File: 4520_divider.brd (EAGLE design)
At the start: 99.4 x 30.5 mm, 54 parts, among them IC1 4520N, IC2 4050N, IC3 78L05Z

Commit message: Moved labels, added top layer ground plane, added alternative 1206 caps in PSU curcuit for use when low-profile electrolytic caps are hard to find.
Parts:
- added C4, C5: 10u, rcl:C1206K
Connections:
- net +5V: now also C5.1
- net GND: now also C4.2, C5.2
- net N$7: now also C4.1
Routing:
- net +5V: track 56.7 -> 59.4 mm
- net N$7: track 6.35 -> 9.12 mm
- added copper zone on layer 1, net GND
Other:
- board text added: "RED STRIPE <- -12V here"
- board text removed: "<-RED STRIPE/-12V HERE"
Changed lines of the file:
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@@
 <wire x1="84.455" y1="5.715" x2="84.455" y2="1.905" width="0.254" layer="22"/>
 <wire x1="85.09" y1="6.35" x2="85.09" y2="1.27" width="0.254" layer="22"/>
-<text x="83.185" y="4.445" size="1.27" layer="22" font="vector" rot="SMR0">&lt;-RED STRIPE/-12V HERE</text>
-<text x="81.915" y="18.415" size="1.27" layer="22" font="vector" rot="SMR0">4520 clock divider
+<text x="83.185" y="4.445" size="1.4224" layer="22" font="vector" rot="SMR0">RED STRIPE
+&lt;- -12V here</text>
+<text x="80.645" y="17.78" size="1.016" layer="22" font="vector" rot="SMR0">4520 clock divider
 cc-by-sa 2016
 Lars Bengtsson</text>
@@
 <attribute name="VALUE" x="51.816" y="5.334" size="1.27" layer="27" ratio="10" rot="R180"/>
 </element>
-<element name="D1" library="diode" package="D-2.5" value="" x="96.52" y="7.62"/>
+<element name="D1" library="diode" package="D-2.5" value="" x="96.52" y="7.62" smashed="yes">
+<attribute name="NAME" x="96.774" y="8.763" size="1.27" layer="25" ratio="10"/>
+<attribute name="VALUE" x="94.869" y="5.207" size="1.27" layer="27" ratio="10"/>
+</element>
 <element name="IC1" library="45xx" package="DIL16" value="4520N" x="54.61" y="13.97" smashed="yes" rot="R90">
 <attribute name="NAME" x="57.531" y="3.429" size="1.27" layer="25" ratio="10" rot="R180"/>
 <attribute name="VALUE" x="55.245" y="10.922" size="1.27" layer="25" ratio="10" rot="R90"/>
 </element>
-<element name="IC3" library="linear" package="TO92" value="78L05Z" x="91.44" y="7.62"/>
+<element name="IC3" library="linear" package="TO92" value="78L05Z" x="91.44" y="7.62" smashed="yes">
+<attribute name="NAME" x="88.519" y="6.858" size="1.27" layer="25" ratio="10" rot="R90"/>
+<attribute name="VALUE" x="94.361" y="6.35" size="1.27" layer="27" ratio="10"/>
+</element>
 <element name="JP1" library="pinhead" package="2X05" value="EURORACK PSU" x="91.44" y="3.81" rot="MR0"/>
 <element name="LED1" library="led" package="LED3MM" value="" x="97.79" y="25.4" smashed="yes" rot="R90">
@@
 </element>
 <element name="R1" library="rcl" package="0204V" value="100k" x="80.01" y="13.97" rot="R180"/>
-<element name="R10" library="rcl" package="R1206" value="1k" x="7.62" y="21.59" rot="MR0"/>
-<element name="R11" library="rcl" package="R1206" value="1k" x="4.445" y="10.795" rot="MR0"/>
-<element name="R12" library="rcl" package="R1206" value="10k" x="69.85" y="24.765" rot="MR90"/>
-<element name="R13" library="rcl" package="R1206" value="10k" x="82.55" y="24.765" rot="MR90"/>
-<element name="R14" library="rcl" package="R1206" value="10k" x="95.25" y="24.765" rot="MR90"/>
-<element name="R15" library="rcl" package="0204V" value="100k" x="85.09" y="17.78" rot="R90"/>
+<element name="R10" library="rcl" package="R1206" value="1k" x="7.62" y="21.59" smashed="yes" rot="MR0">
+<attribute name="NAME" x="9.525" y="19.05" size="1.27" layer="26" rot="MR0"/>
+<attribute name="VALUE" x="8.89" y="19.05" size="1.27" layer="28" rot="MR0"/>
+</element>
+<element name="R11" library="rcl" package="R1206" value="1k" x="4.445" y="10.795" smashed="yes" rot="MR0">
+<attribute name="NAME" x="6.985" y="8.255" size="1.27" layer="26" rot="MR0"/>
+<attribute name="VALUE" x="5.715" y="8.255" size="1.27" layer="28" rot="MR0"/>
+</element>
+<element name="R12" library="rcl" package="R1206" value="10k" x="69.85" y="24.765" smashed="yes" rot="MR90">
+<attribute name="NAME" x="67.31" y="23.495" size="1.27" layer="26" rot="MR90"/>
+<attribute name="VALUE" x="67.31" y="23.495" size="1.27" layer="28" rot="MR90"/>
+</element>
+<element name="R13" library="rcl" package="R1206" value="10k" x="82.55" y="24.765" smashed="yes" rot="MR90">
+<attribute name="NAME" x="80.01" y="23.495" size="1.27" layer="26" rot="MR90"/>
+<attribute name="VALUE" x="80.01" y="23.495" size="1.27" layer="28" rot="MR90"/>
+</element>
+<element name="R14" library="rcl" package="R1206" value="10k" x="95.25" y="24.765" smashed="yes" rot="MR90">
+<attribute name="NAME" x="92.71" y="23.495" size="1.27" layer="26" rot="MR90"/>
+<attribute name="VALUE" x="92.71" y="23.495" size="1.27" layer="28" rot="MR90"/>
+</element>
+<element name="R15" library="rcl" package="0204V" value="100k" x="85.09" y="17.78" smashed="yes" rot="R90">
+<attribute name="NAME" x="85.8266" y="20.0914" size="1.27" layer="25" ratio="10" rot="R90"/>
+<attribute name="VALUE" x="87.4014" y="15.6464" size="1.27" layer="27" ratio="10" rot="R90"/>
+</element>
 <element name="R16" library="rcl" package="R1206" value="10k" x="43.815" y="26.035" rot="MR90"/>
 <element name="R17" library="rcl" package="R1206" value="10k" x="44.45" y="16.51" rot="MR270"/>
@@
 <element name="R23" library="rcl" package="R1206" value="10k" x="6.35" y="16.51" rot="MR270"/>
 <element name="R3" library="rcl" package="0204V" value="100k" x="67.31" y="13.97" rot="R180"/>
-<element name="R4" library="rcl" package="R1206" value="1k" x="45.72" y="21.59" rot="MR0"/>
-<element name="R5" library="rcl" package="R1206" value="1k" x="42.545" y="10.795" rot="MR0"/>
-<element name="R6" library="rcl" package="R1206" value="1k" x="33.02" y="21.59" rot="MR0"/>
-<element name="R7" library="rcl" package="R1206" value="1k" x="29.845" y="10.795" rot="MR0"/>
-<element name="R8" library="rcl" package="R1206" value="1k" x="20.32" y="21.59" rot="MR0"/>
-<element name="R9" library="rcl" package="R1206" value="1k" x="17.145" y="10.795" rot="MR0"/>
+<element name="R4" library="rcl" package="R1206" value="1k" x="45.72" y="21.59" smashed="yes" rot="MR0">
+<attribute name="NAME" x="48.26" y="19.05" size="1.27" layer="26" rot="MR0"/>
+<attribute name="VALUE" x="46.99" y="19.05" size="1.27" layer="28" rot="MR0"/>
+</element>
+<element name="R5" library="rcl" package="R1206" value="1k" x="42.545" y="10.795" smashed="yes" rot="MR0">
+<attribute name="NAME" x="45.085" y="8.255" size="1.27" layer="26" rot="MR0"/>
+<attribute name="VALUE" x="43.815" y="8.255" size="1.27" layer="28" rot="MR0"/>
+</element>
+<element name="R6" library="rcl" package="R1206" value="1k" x="33.02" y="21.59" smashed="yes" rot="MR0">
+<attribute name="NAME" x="34.29" y="19.05" size="1.27" layer="26" rot="MR0"/>
+<attribute name="VALUE" x="34.29" y="19.05" size="1.27" layer="28" rot="MR0"/>
+</element>
+<element name="R7" library="rcl" package="R1206" value="1k" x="29.845" y="10.795" smashed="yes" rot="MR0">
+<attribute name="NAME" x="32.385" y="8.255" size="1.27" layer="26" rot="MR0"/>
+<attribute name="VALUE" x="31.115" y="8.255" size="1.27" layer="28" rot="MR0"/>
+</element>
+<element name="R8" library="rcl" package="R1206" value="1k" x="20.32" y="21.59" smashed="yes" rot="MR0">
+<attribute name="NAME" x="22.86" y="19.05" size="1.27" layer="26" rot="MR0"/>
+<attribute name="VALUE" x="21.59" y="19.05" size="1.27" layer="28" rot="MR0"/>
+</element>
+<element name="R9" library="rcl" package="R1206" value="1k" x="17.145" y="10.795" smashed="yes" rot="MR0">
+<attribute name="NAME" x="19.685" y="8.255" size="1.27" layer="26" rot="MR0"/>
+<attribute name="VALUE" x="18.415" y="8.255" size="1.27" layer="28" rot="MR0"/>
+</element>
 <element name="CLK" library="thonkiconn" package="WQP-PJ301M-12_JACK" value="WQP-PJ301M-12_JACK" x="91.44" y="21.59" smashed="yes" rot="R180">
 <attribute name="NAME" x="92.6846" y="28.2448" size="1.27" layer="21"/>
@@
 </element>
 <element name="C1" library="rcl" package="E2,5-5" value="10u" x="95.25" y="12.7" smashed="yes" rot="R90">
-<attribute name="NAME" x="93.98" y="15.113" size="1.27" layer="25" ratio="10" rot="R90"/>
+<attribute name="NAME" x="98.425" y="13.843" size="1.27" layer="25" ratio="10" rot="R90"/>
 <attribute name="VALUE" x="97.663" y="15.113" size="1.27" layer="27" ratio="10" rot="R90"/>
 </element>
 <element name="C3" library="rcl" package="E2,5-5" value="10u" x="88.265" y="12.7" smashed="yes" rot="R90">
-<attribute name="NAME" x="86.995" y="15.113" size="1.27" layer="25" ratio="10" rot="R90"/>
+<attribute name="NAME" x="85.725" y="13.208" size="1.27" layer="25" ratio="10" rot="R90"/>
 <attribute name="VALUE" x="90.678" y="15.113" size="1.27" layer="27" ratio="10" rot="R90"/>
 </element>
+<element name="C4" library="rcl" package="C1206K" value="10u" x="97.79" y="12.7" rot="MR90"/>
+<element name="C5" library="rcl" package="C1206K" value="10u" x="90.805" y="12.7" rot="MR90"/>
 </elements>
 <signals>
@@
 <contactref element="R18" pad="1"/>
 <contactref element="R17" pad="1"/>
-<polygon width="0.3048" layer="16" isolate="0.4064">
+<polygon width="0.254" layer="16" isolate="0.4064">
 <vertex x="0.635" y="29.845"/>
 <vertex x="99.06" y="29.845"/>
@@
 <contactref element="C1" pad="-"/>
 <contactref element="C3" pad="-"/>
+<contactref element="C4" pad="2"/>
+<contactref element="C5" pad="2"/>
+<polygon width="0.254" layer="1" isolate="0.254">
+<vertex x="0.635" y="29.845"/>
+<vertex x="99.06" y="29.845"/>
+<vertex x="99.06" y="0.635"/>
+<vertex x="0.635" y="0.635"/>
+</polygon>
+<via x="34.29" y="15.875" extent="1-16" drill="0.6" shape="square"/>
+<via x="36.195" y="10.16" extent="1-16" drill="0.6" shape="square"/>
+<via x="53.34" y="15.24" extent="1-16" drill="0.6" shape="square"/>
 </signal>
 <signal name="N$3">
@@
 <wire x1="85.09" y1="13.97" x2="83.82" y2="12.7" width="0.254" layer="16"/>
 <wire x1="83.82" y1="12.7" x2="83.82" y2="10.16" width="0.254" layer="16"/>
+<contactref element="C5" pad="1"/>
+<wire x1="88.265" y1="11.43" x2="90.805" y2="11.43" width="0.8128" layer="16"/>
+<wire x1="90.805" y1="11.43" x2="90.805" y2="11.2" width="0.8128" layer="16"/>
 </signal>
 <signal name="+12V_IN">
@@
 <wire x1="95.25" y1="7.62" x2="95.25" y2="11.43" width="0.8128" layer="1"/>
 <wire x1="92.71" y1="7.62" x2="95.25" y2="7.62" width="0.8128" layer="1"/>
+<contactref element="C4" pad="1"/>
+<wire x1="95.25" y1="11.43" x2="97.79" y2="11.43" width="0.8128" layer="16"/>
+<wire x1="97.79" y1="11.43" x2="97.79" y2="11.2" width="0.8128" layer="16"/>
 </signal>
 <signal name="N$26">

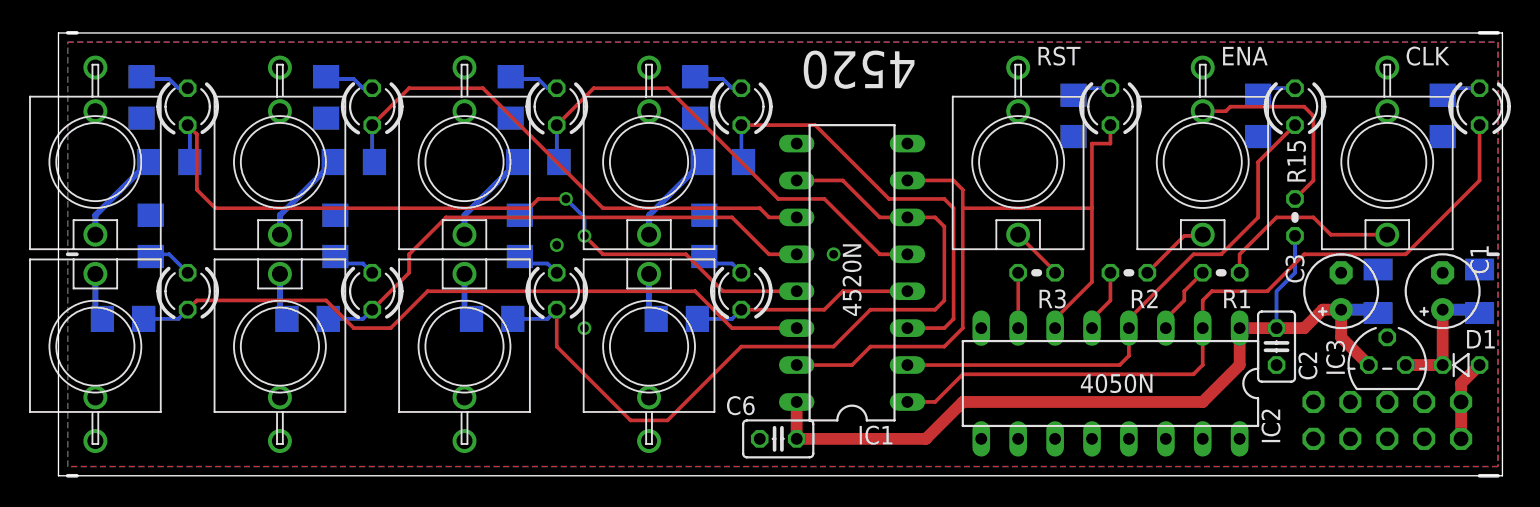
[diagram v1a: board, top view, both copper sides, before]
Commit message: Trimmed borders a bit.
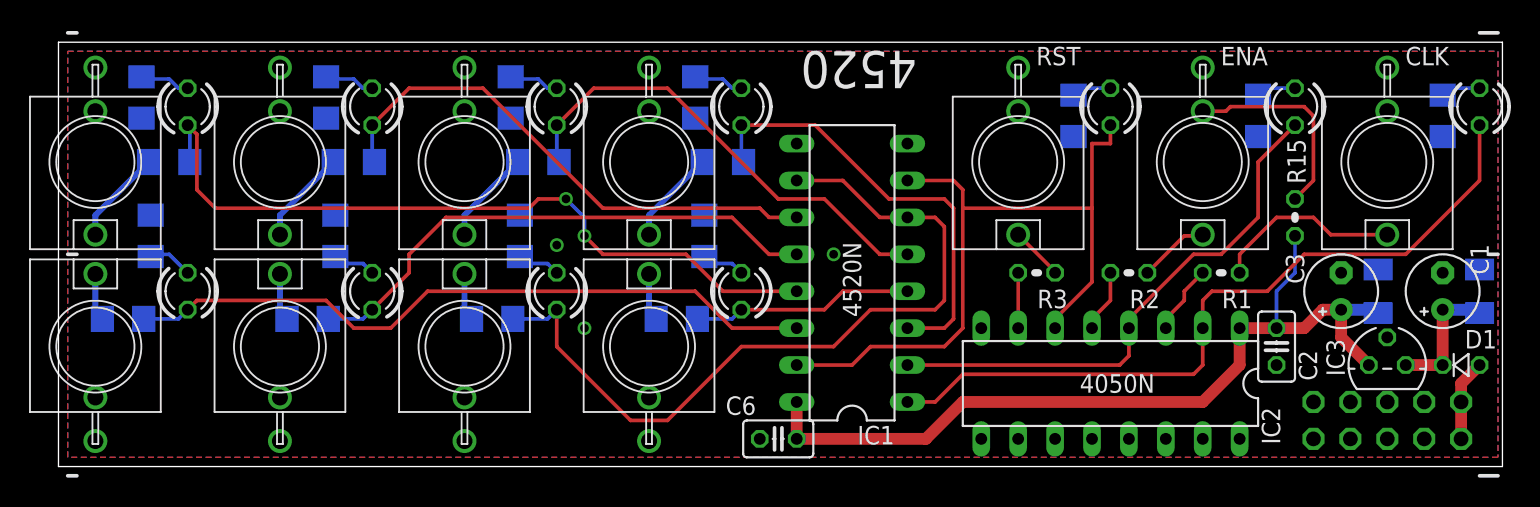
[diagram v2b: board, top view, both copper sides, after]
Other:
- board size 99.4 x 30.5 mm -> 99.4 x 29.2 mm
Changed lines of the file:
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@@
 <board>
 <plain>
-<wire x1="0" y1="0" x2="99.365" y2="0" width="0" layer="20"/>
-<wire x1="99.365" y1="0" x2="99.365" y2="30.47" width="0" layer="20"/>
-<wire x1="99.365" y1="30.47" x2="0" y2="30.47" width="0" layer="20"/>
-<wire x1="0" y1="30.47" x2="0" y2="0" width="0" layer="20"/>
+<wire x1="0" y1="0.635" x2="99.365" y2="0.635" width="0" layer="20"/>
+<wire x1="99.365" y1="0.635" x2="99.365" y2="29.835" width="0" layer="20"/>
+<wire x1="99.365" y1="29.835" x2="0" y2="29.835" width="0" layer="20"/>
+<wire x1="0" y1="29.835" x2="0" y2="0.635" width="0" layer="20"/>
 <wire x1="0.635" y1="0" x2="1.27" y2="0" width="0.254" layer="21"/>
 <wire x1="0.635" y1="15.24" x2="1.27" y2="15.24" width="0.254" layer="21"/>
@@
 <attribute name="VALUE" x="90.678" y="15.113" size="1.27" layer="27" ratio="10" rot="R90"/>
 </element>
-<element name="C4" library="rcl" package="C1206K" value="10u" x="97.79" y="12.7" rot="MR90"/>
-<element name="C5" library="rcl" package="C1206K" value="10u" x="90.805" y="12.7" rot="MR90"/>
+<element name="C4" library="rcl" package="C1206K" value="10u" x="97.79" y="12.7" smashed="yes" rot="MR90">
+<attribute name="NAME" x="96.35" y="14.91" size="1.016" layer="26" rot="MR90"/>
+<attribute name="VALUE" x="95.69" y="11.1" size="1.016" layer="28" rot="MR90"/>
+</element>
+<element name="C5" library="rcl" package="C1206K" value="10u" x="90.805" y="12.7" smashed="yes" rot="MR90">
+<attribute name="NAME" x="89.365" y="14.91" size="1.016" layer="26" rot="MR90"/>
+<attribute name="VALUE" x="88.705" y="11.1" size="1.016" layer="28" rot="MR90"/>
+</element>
 </elements>
 <signals>
@@
 <contactref element="R17" pad="1"/>
 <polygon width="0.254" layer="16" isolate="0.4064">
-<vertex x="0.635" y="29.845"/>
-<vertex x="99.06" y="29.845"/>
-<vertex x="99.06" y="0.635"/>
-<vertex x="0.635" y="0.635"/>
+<vertex x="0.635" y="29.21"/>
+<vertex x="99.06" y="29.21"/>
+<vertex x="99.06" y="1.27"/>
+<vertex x="0.635" y="1.27"/>
 </polygon>
 <contactref element="IC2" pad="8"/>
@@
 <contactref element="C5" pad="2"/>
 <polygon width="0.254" layer="1" isolate="0.254">
-<vertex x="0.635" y="29.845"/>
-<vertex x="99.06" y="29.845"/>
-<vertex x="99.06" y="0.635"/>
-<vertex x="0.635" y="0.635"/>
+<vertex x="0.635" y="29.21"/>
+<vertex x="99.06" y="29.21"/>
+<vertex x="99.06" y="1.27"/>
+<vertex x="0.635" y="1.27"/>
 </polygon>
 <via x="34.29" y="15.875" extent="1-16" drill="0.6" shape="square"/>
